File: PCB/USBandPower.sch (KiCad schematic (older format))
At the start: 16 parts, among them J3 USB_B_Micro, J4 12V 1A IN (5.5/2.5), J5 12V IN, U2 FT232RL, U3 LM2940

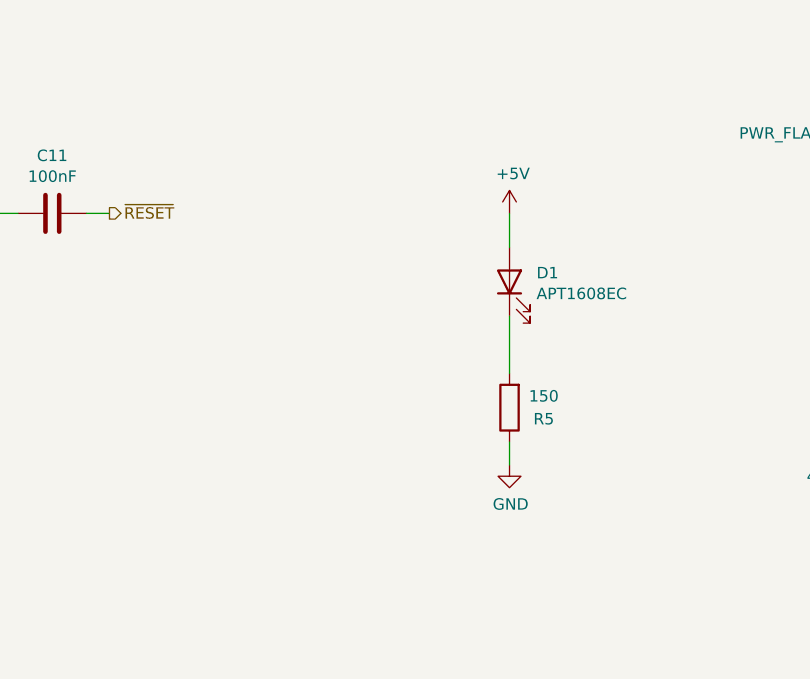
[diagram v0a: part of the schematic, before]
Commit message: Added LED for 12V power. Added resistor on MPS_STIMULUS signal. Moved track away from mounting hole. Fixed orientation of diodes. Added PDF of schematic. Updated manufacturing files.
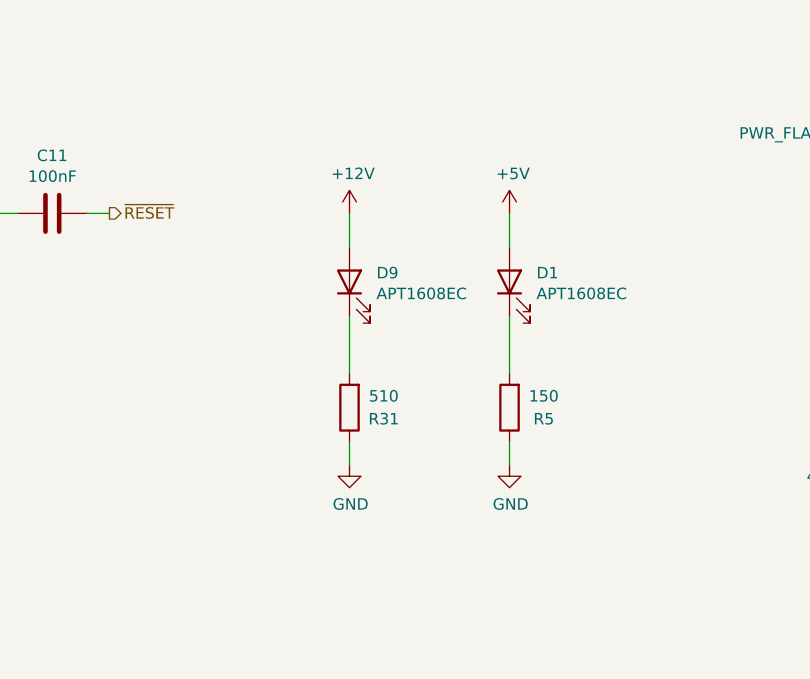
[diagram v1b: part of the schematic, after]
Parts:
- added D9: APT1608EC, LED_SMD:LED_0603_1608Metric, symbol Device:LED
- added R31: 510, Resistor_SMD:R_0603_1608Metric, symbol Device:R
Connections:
- net +12V: now also D9.2 (A)
- net GND: now also R31.1
- new net: D9.1 (K), R31.2
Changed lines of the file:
@@
 Sheet 2 3
 Title "MPS Tune-o-Matic"
-Date "2022-10-31"
-Rev "V1.0"
+Date "2022-11-10"
+Rev "V1.1"
 Comp "(C) andy@britishideas.com 2022"
 Comment1 "For Bosch D-Jetronic MPS Type 3"
@@
 	1    0    0    -1
 $EndComp
+$Comp
+L Device:LED D?
+U 1 1 636F0574
+P 6750 2350
+AR Path="/636F0574" Ref="D?"  Part="1"
+AR Path="/60479334/636F0574" Ref="D9"  Part="1"
+F 0 "D9" V 6789 2232 50  0000 R CNN
+F 1 "APT1608EC" V 6698 2232 50  0000 R CNN
+F 2 "LED_SMD:LED_0603_1608Metric" H 6750 2350 50  0001 C CNN
+F 3 "~" H 6750 2350 50  0001 C CNN
+F 4 "APT1608EC" V 6750 2350 50  0001 C CNN "manf#"
+	1    6750 2350
+	0    -1   -1   0
+$EndComp
+$Comp
+L Device:R R?
+U 1 1 636F0836
+P 6750 2900
+AR Path="/636F0836" Ref="R?"  Part="1"
+AR Path="/60479334/636F0836" Ref="R31"  Part="1"
+F 0 "R31" H 6600 2950 50  0000 C CNN
+F 1 "510" H 6600 2850 50  0000 C CNN
+F 2 "Resistor_SMD:R_0603_1608Metric" V 6680 2900 50  0001 C CNN
+F 3 "~" H 6750 2900 50  0001 C CNN
+	1    6750 2900
+	-1   0    0    1
+$EndComp
+$Comp
+L power:GND #PWR?
+U 1 1 636F0840
+P 6750 3150
+AR Path="/636F0840" Ref="#PWR?"  Part="1"
+AR Path="/60479334/636F0840" Ref="#PWR039"  Part="1"
+F 0 "#PWR039" H 6750 2900 50  0001 C CNN
+F 1 "GND" H 6755 2977 50  0000 C CNN
+F 2 "" H 6750 3150 50  0001 C CNN
+F 3 "" H 6750 3150 50  0001 C CNN
+	1    6750 3150
+	1    0    0    -1
+$EndComp
+Wire Wire Line
+	6750 2500 6750 2750
+Wire Wire Line
+	6750 3050 6750 3150
+Wire Wire Line
+	6750 2050 6750 2200
+$Comp
+L power:+12V #PWR?
+U 1 1 636F3AD7
+P 6750 2050
+AR Path="/636F3AD7" Ref="#PWR?"  Part="1"
+AR Path="/60479334/636F3AD7" Ref="#PWR038"  Part="1"
+F 0 "#PWR038" H 6750 1900 50  0001 C CNN
+F 1 "+12V" H 6765 2223 50  0000 C CNN
+F 2 "" H 6750 2050 50  0001 C CNN
+F 3 "" H 6750 2050 50  0001 C CNN
+	1    6750 2050
+	1    0    0    -1
+$EndComp
